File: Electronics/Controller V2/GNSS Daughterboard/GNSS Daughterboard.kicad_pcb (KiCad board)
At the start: 2 copper layers, 76 x 70.5 mm, 13 parts, among them J1 GNSS, J2 Conn_01x02, J3 Conn_01x02, J4 Conn_01x02, J5 Conn_01x02, J6 Conn_01x02, J7 Conn_01x02, J8 GNSS, U1 simpleRTK2B

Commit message: Completed daughterboards.
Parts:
- H1, H2, H3, H4: footprint MountingHole:MountingHole_3.2mm_M3 -> MountingHole:MountingHole_6.4mm_M6
- moved H1 5.32 mm to (180.0, 57.0)
- moved H2 4.30 mm to (105.5, 57.0)
- moved H3 4.27 mm to (180.0, 117.5)
- moved H4 2.92 mm to (105.5, 117.5)
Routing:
- net /GNSS_B_TX: track 59.4 -> 55.6 mm, vias 1 -> 0
- net GND: vias 173 -> 15
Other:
- board size 76 x 70.5 mm -> 88.5 x 74.5 mm

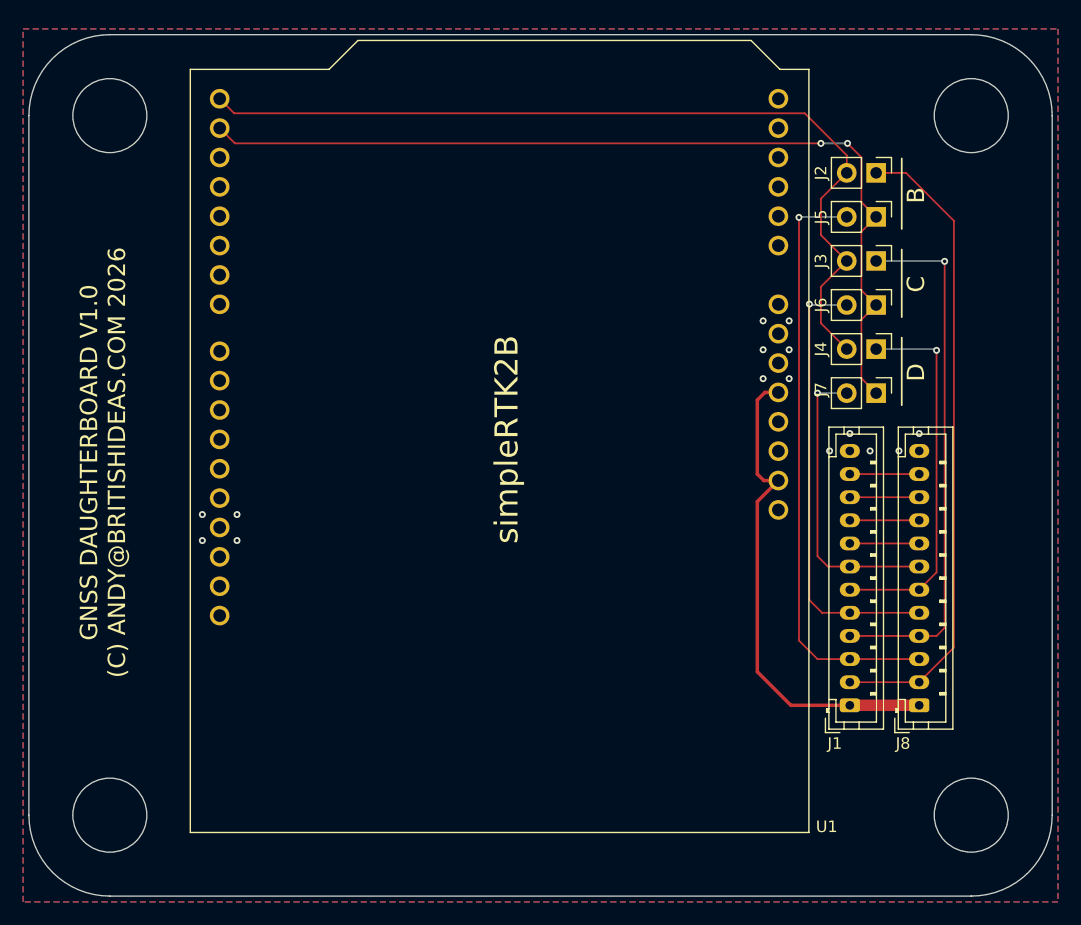
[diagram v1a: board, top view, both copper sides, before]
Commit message: Working on motherboard layout. Added SMA adapters to GNSS daughterboard. Generated CAD files.
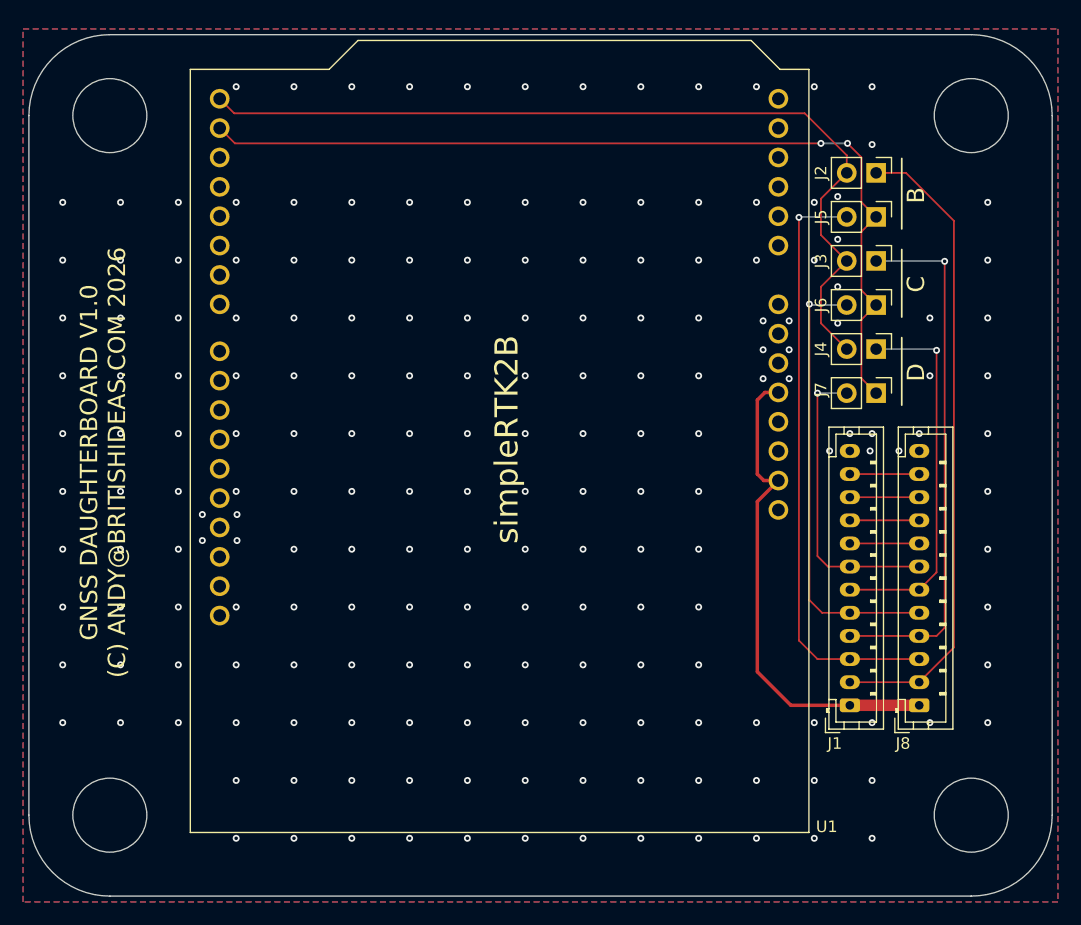
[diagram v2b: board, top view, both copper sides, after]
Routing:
- net GND: vias 15 -> 196

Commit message: Added jumper to bypass current sensing. Minor tweaks. Generated production files.
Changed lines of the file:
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@@
     (fp_line (start 23.95 2.8) (end 23.95 -1.7)
       (stroke (width 0.1) (type solid)) (layer "F.Fab"))
-    (pad "1" thru_hole roundrect (at 0 0 90) (size 1.2 1.75) (drill 0.75) (layers "*.Cu" "*.Mask") (roundrect_rratio 0.208333)
+    (pad "1" thru_hole roundrect (at 0 0 90) (size 1.2 1.75) (drill 0.75) (layers "*.Cu" "*.Mask") (roundrect_rratio 0.2083333333)
       (net 1 "+5V") (pinfunction "Pin_1") (pintype "passive"))
     (pad "2" thru_hole oval (at 2 0 90) (size 1.2 1.75) (drill 0.75) (layers "*.Cu" "*.Mask")
@@
     (fp_line (start 23.95 2.8) (end 23.95 -1.7)
       (stroke (width 0.1) (type solid)) (layer "F.Fab"))
-    (pad "1" thru_hole roundrect (at 0 0 90) (size 1.2 1.75) (drill 0.75) (layers "*.Cu" "*.Mask") (roundrect_rratio 0.208333)
+    (pad "1" thru_hole roundrect (at 0 0 90) (size 1.2 1.75) (drill 0.75) (layers "*.Cu" "*.Mask") (roundrect_rratio 0.2083333333)
       (net 1 "+5V") (pinfunction "Pin_1") (pintype "passive"))
     (pad "2" thru_hole oval (at 2 0 90) (size 1.2 1.75) (drill 0.75) (layers "*.Cu" "*.Mask")
